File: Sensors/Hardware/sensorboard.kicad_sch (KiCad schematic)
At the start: 75 parts, among them J15 Conn_Coaxial, U3 TPS61092RSAR

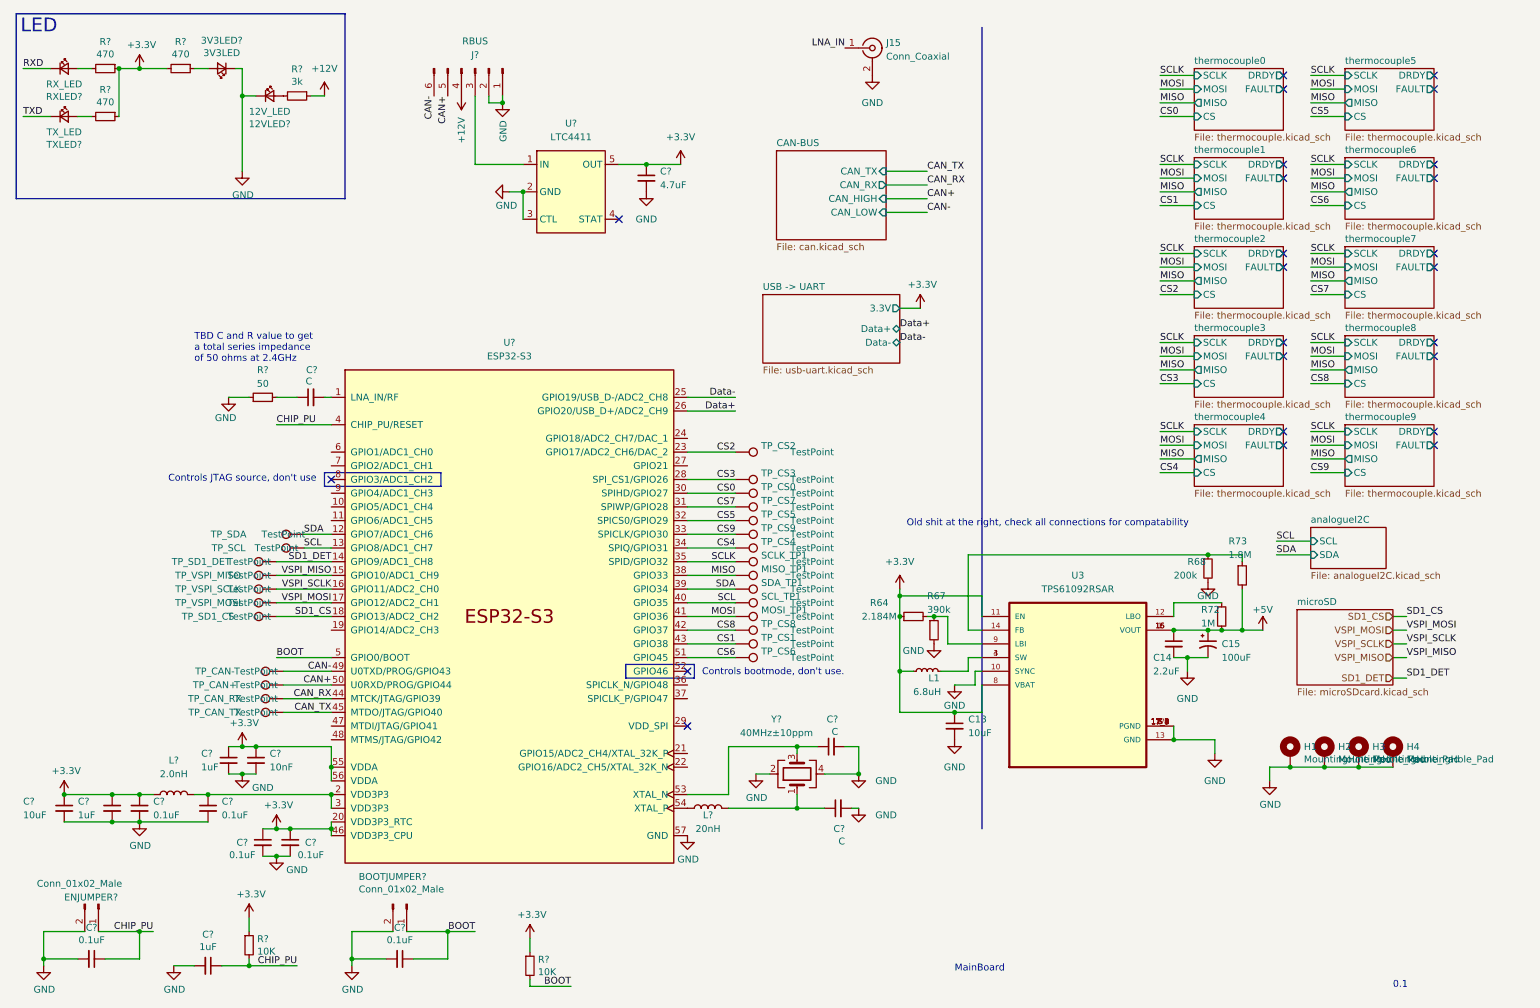
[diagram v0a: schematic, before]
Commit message: removed thermocouples
updated connections
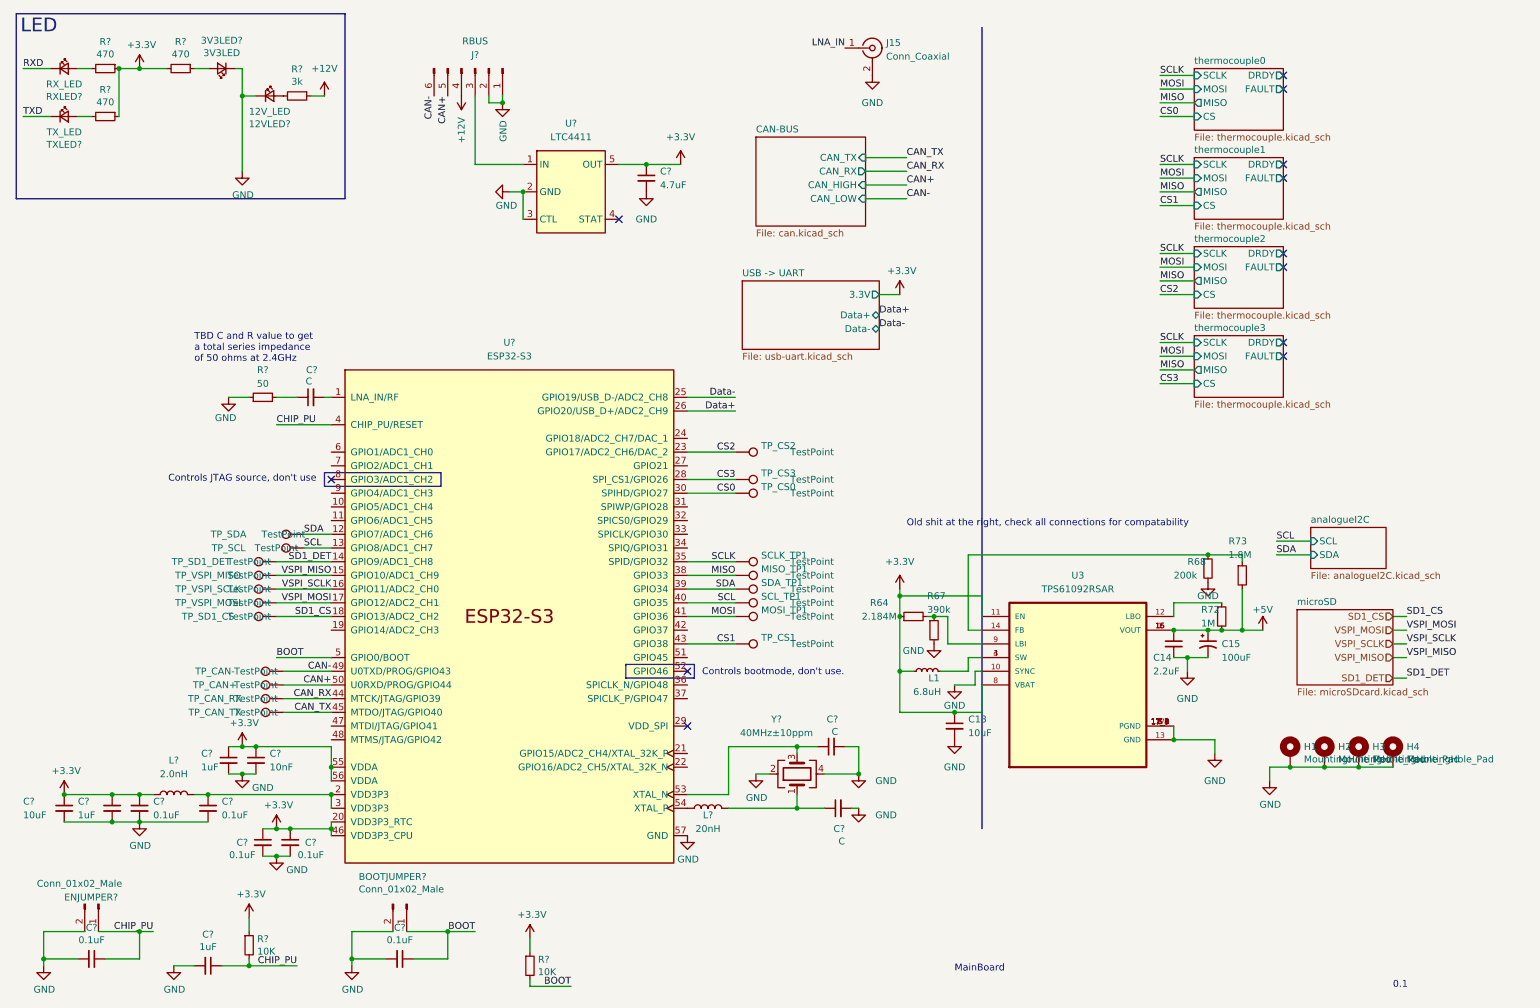
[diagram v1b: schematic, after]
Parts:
- removed TP_CS4, TP_CS5, TP_CS6, TP_CS7, TP_CS8, TP_CS9: TestPoint, TestPoint:TestPoint_Pad_D1.0mm, symbol Connector:TestPoint
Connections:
- net CS4: no longer names the net of U?.34 (SPIQ/GPIO31)
- net CS5: no longer names the net of U?.32 (SPICS0/GPIO29)
- net CS6: no longer names the net of U?.51 (GPIO45)
- net CS7: no longer names the net of U?.31 (SPIWP/GPIO28)
- net CS8: no longer names the net of U?.42 (GPIO37)
- net CS9: no longer names the net of U?.33 (SPICLK/GPIO30)
- no-connect marks 24 -> 12
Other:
- removed sheet thermocouple4
- removed sheet thermocouple5
- removed sheet thermocouple6
- removed sheet thermocouple7
- removed sheet thermocouple8
- removed sheet thermocouple9

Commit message: added new ADC and some connections
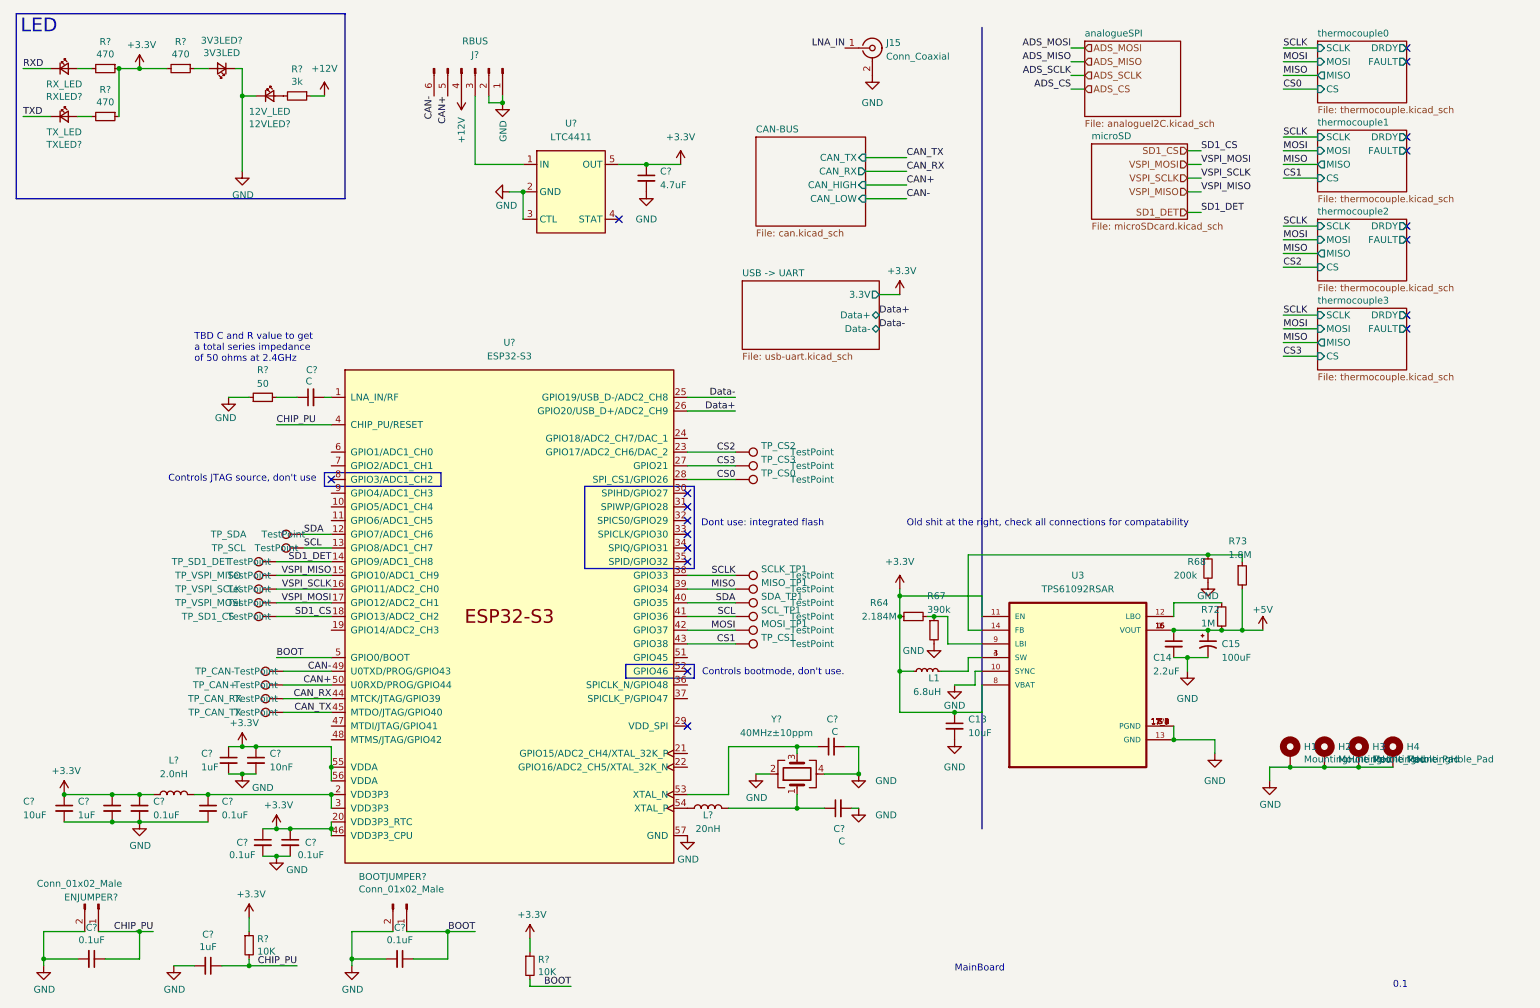
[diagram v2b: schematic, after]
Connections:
- net CS0: now also U?.28 (SPI_CS1/GPIO26); no longer U?.30 (SPIHD/GPIO27)
- net CS3: now also U?.27 (GPIO21); no longer U?.28 (SPI_CS1/GPIO26)
- net MISO: now also U?.39 (GPIO34); no longer U?.38 (GPIO33)
- net MOSI: now also U?.42 (GPIO37); no longer U?.41 (GPIO36)
- net SCL: now also U?.41 (GPIO36); no longer U?.40 (GPIO35)
- net SCLK: now also U?.38 (GPIO33); no longer U?.35 (SPID/GPIO32)
- net SDA: now also U?.40 (GPIO35); no longer U?.39 (GPIO34)
- no-connect marks 12 -> 18
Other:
- sheet analogueI2C renamed analogueSPI
- sheet analogueSPI ports: added none; removed SCL, SDA
- note added: "Dont use: integrated flash"
- moved on the sheet: MISO_TP1, MOSI_TP1, SCLK_TP1, SCL_TP1, SDA_TP1, TP_CS0, TP_CS3

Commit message: connectors and update
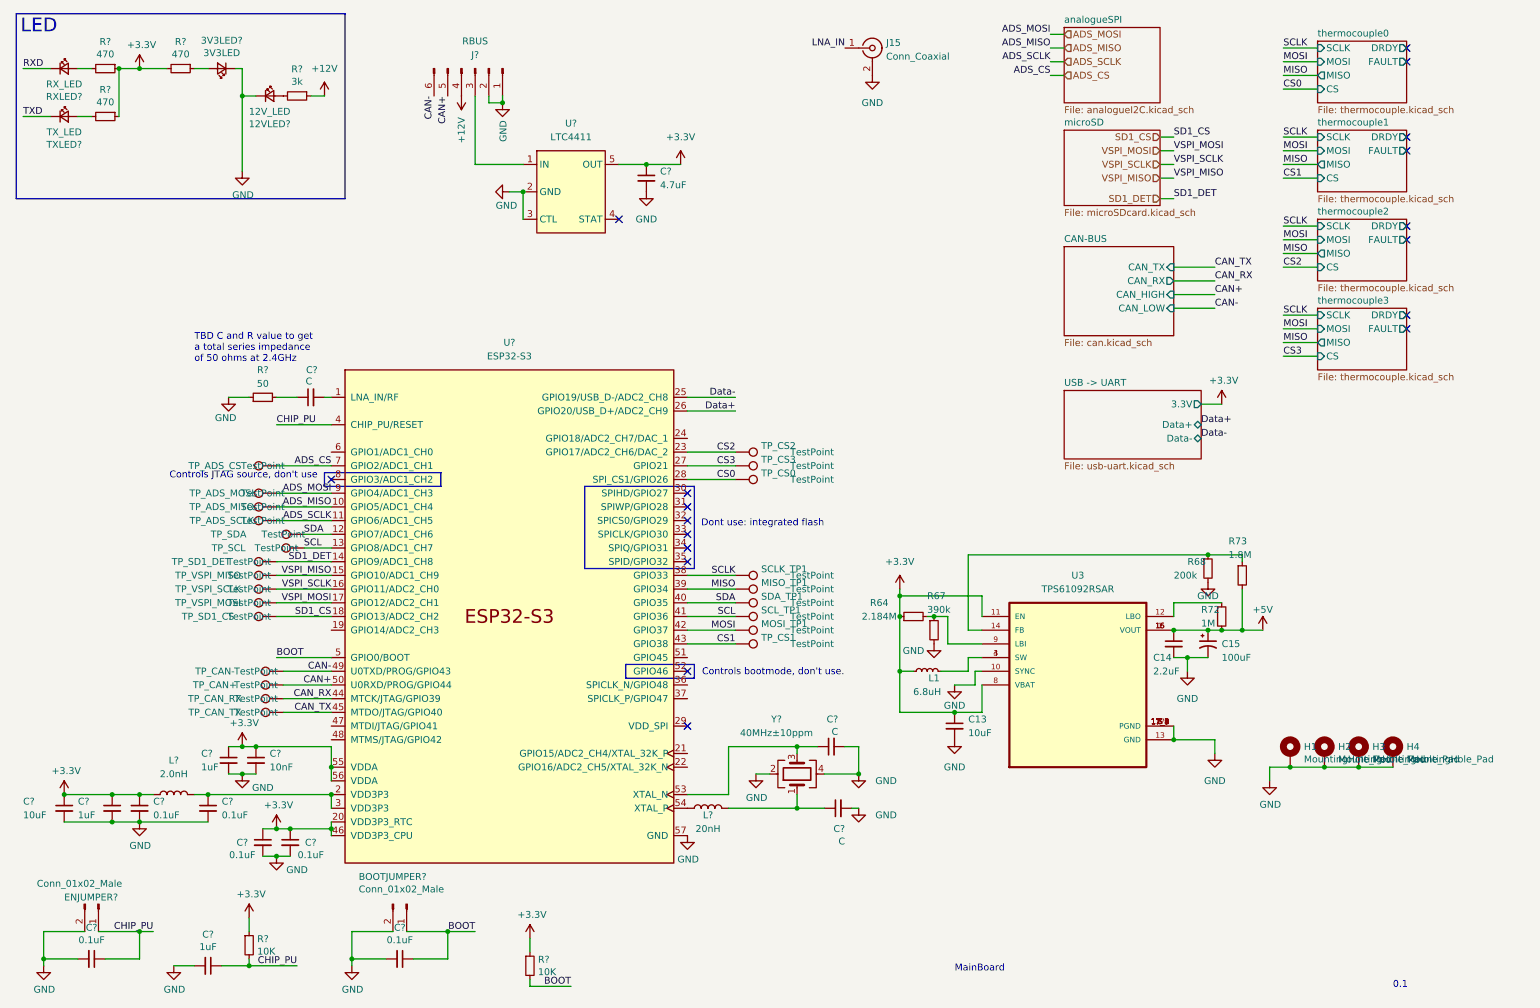
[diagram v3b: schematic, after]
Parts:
- added TP_ADS_CS, TP_ADS_MISO, TP_ADS_MOSI, TP_ADS_SCLK: TestPoint, symbol Connector:TestPoint
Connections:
- net ADS_CS: now also U?.7 (GPIO2/ADC1_CH1), TP_ADS_CS.1
- net ADS_MISO: now also U?.10 (GPIO5/ADC1_CH4), TP_ADS_MISO.1
- net ADS_MOSI: now also U?.9 (GPIO4/ADC1_CH3), TP_ADS_MOSI.1
- net ADS_SCLK: now also U?.11 (GPIO6/ADC1_CH5), TP_ADS_SCLK.1
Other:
- note removed: "Old shit at the right, check all connections for compatability"

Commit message: values for ADC caps and connector circuits
ADC cap values based on assumptions
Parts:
- added TP_ADS_CLK: TestPoint, symbol Connector:TestPoint
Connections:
- net ADS_CLK: now reaches U?.51 (GPIO45)
- net ADS_CLK: now also TP_ADS_CLK.1

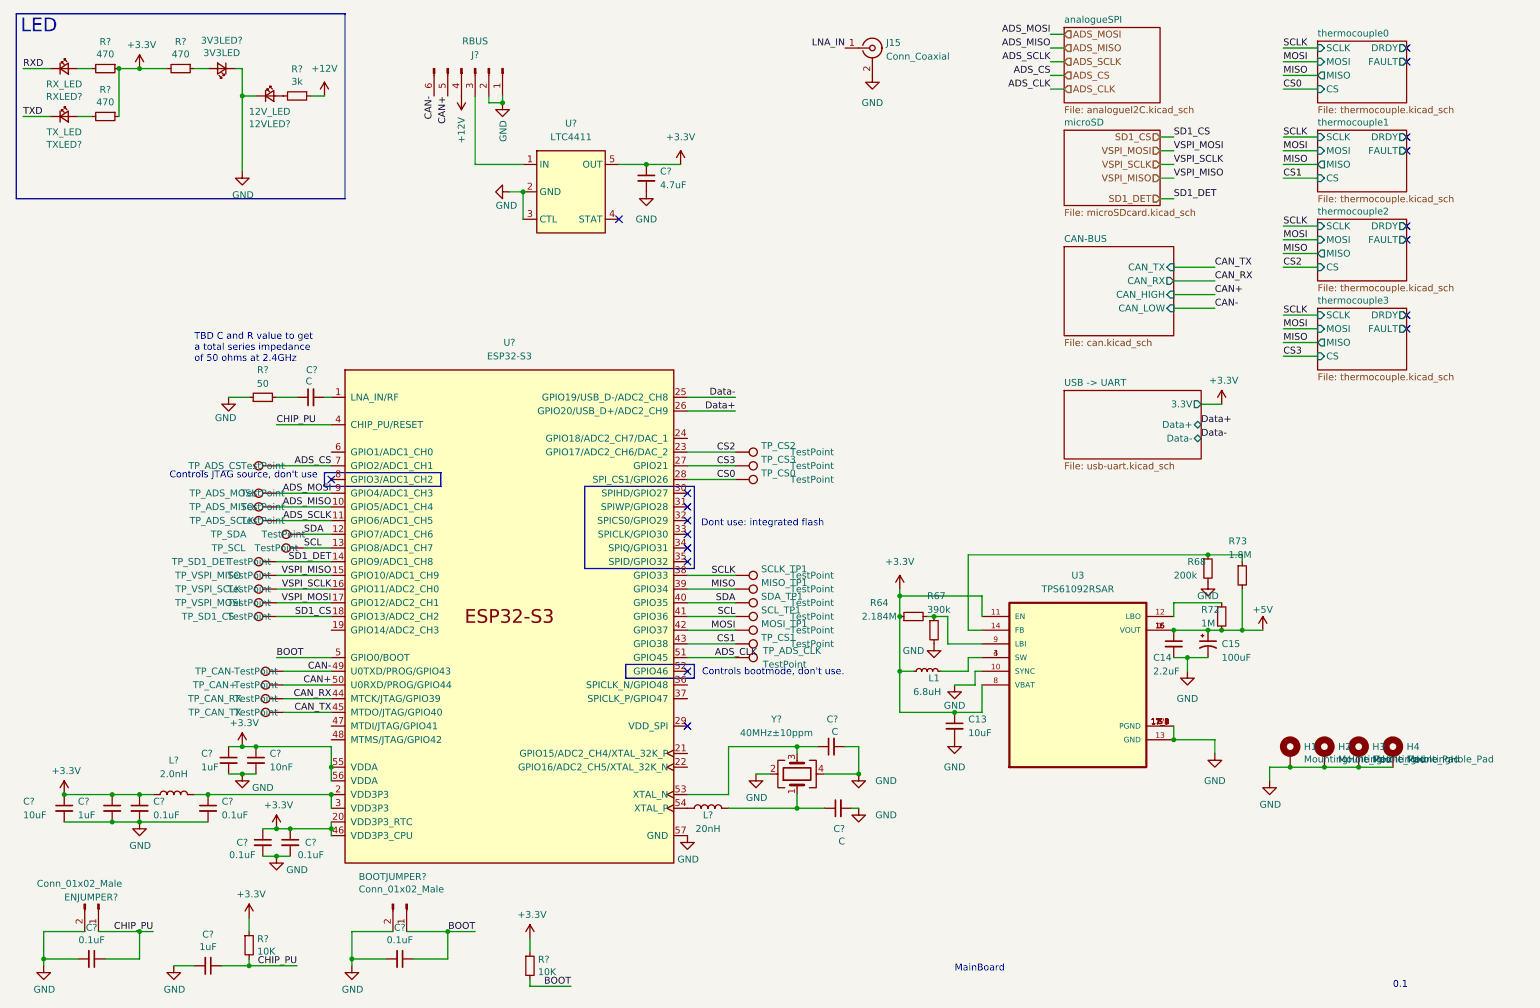
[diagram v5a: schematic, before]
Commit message: fixed hierarchical labels and added ref values
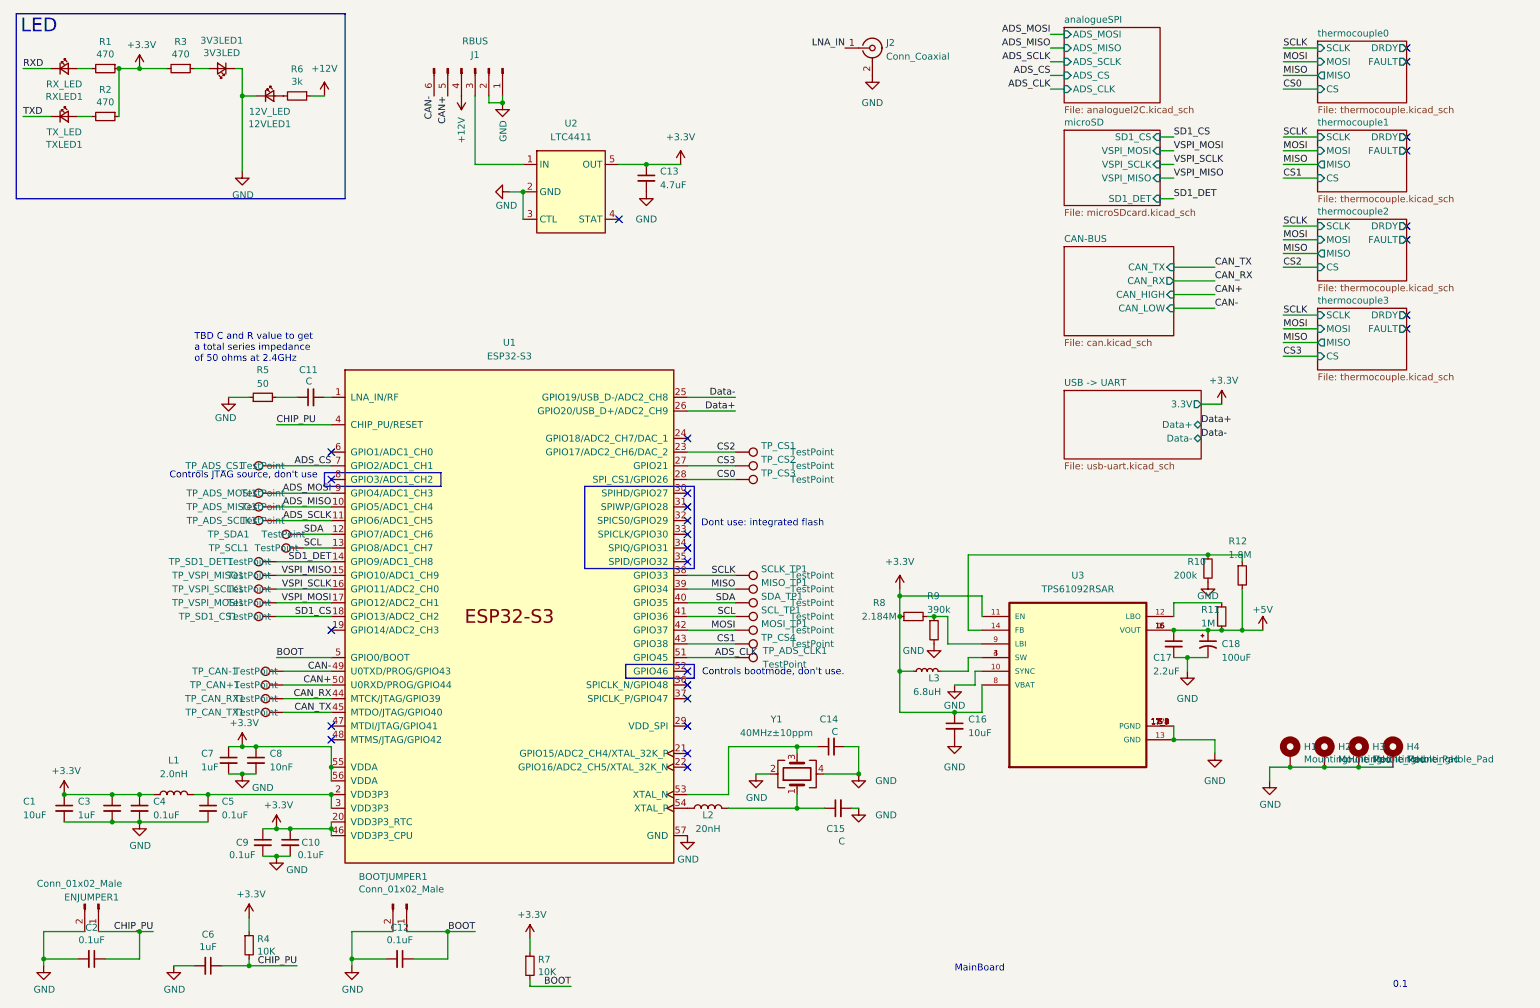
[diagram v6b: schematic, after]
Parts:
- gave numbers to parts that had none: 34
- renumbered C13 to C16, C14 to C17, C15 to C18, J15 to J2, L1 to L3, R68 to R10, R72 to R11, R73 to R12, R64 to R8, R67 to R9, TP_ADS_CLK to TP_ADS_CLK1, TP_ADS_CS to TP_ADS_CS1, TP_ADS_MISO to TP_ADS_MISO1, TP_ADS_MOSI to TP_ADS_MOSI1, TP_ADS_SCLK to TP_ADS_SCLK1, TP_CAN+ to TP_CAN+1, TP_CAN- to TP_CAN-1, TP_CAN_RX to TP_CAN_RX1, TP_CAN_TX to TP_CAN_TX1, TP_CS2 to TP_CS1, TP_CS3 to TP_CS2, TP_CS0 to TP_CS3, TP_CS1 to TP_CS4, TP_SCL to TP_SCL1, TP_SD1_CS to TP_SD1_CS1, TP_SD1_DET to TP_SD1_DET1, TP_SDA to TP_SDA1, TP_VSPI_MISO to TP_VSPI_MISO1, TP_VSPI_MOSI to TP_VSPI_MOSI1, TP_VSPI_SCLK to TP_VSPI_SCLK1
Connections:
- no-connect marks 18 -> 27
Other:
- sheet analogueSPI ports: added ADS_CLK, ADS_CS, ADS_MISO, ADS_MOSI, ADS_SCLK; removed none
- sheet microSD ports: added SD1_CS, SD1_DET, VSPI_MISO, VSPI_MOSI, VSPI_SCLK; removed none
